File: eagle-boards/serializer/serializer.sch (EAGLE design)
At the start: 8 parts, among them IC1 74LS93N, IC2 74LS151N, IC3 74LS86N, IC4 74LS04N

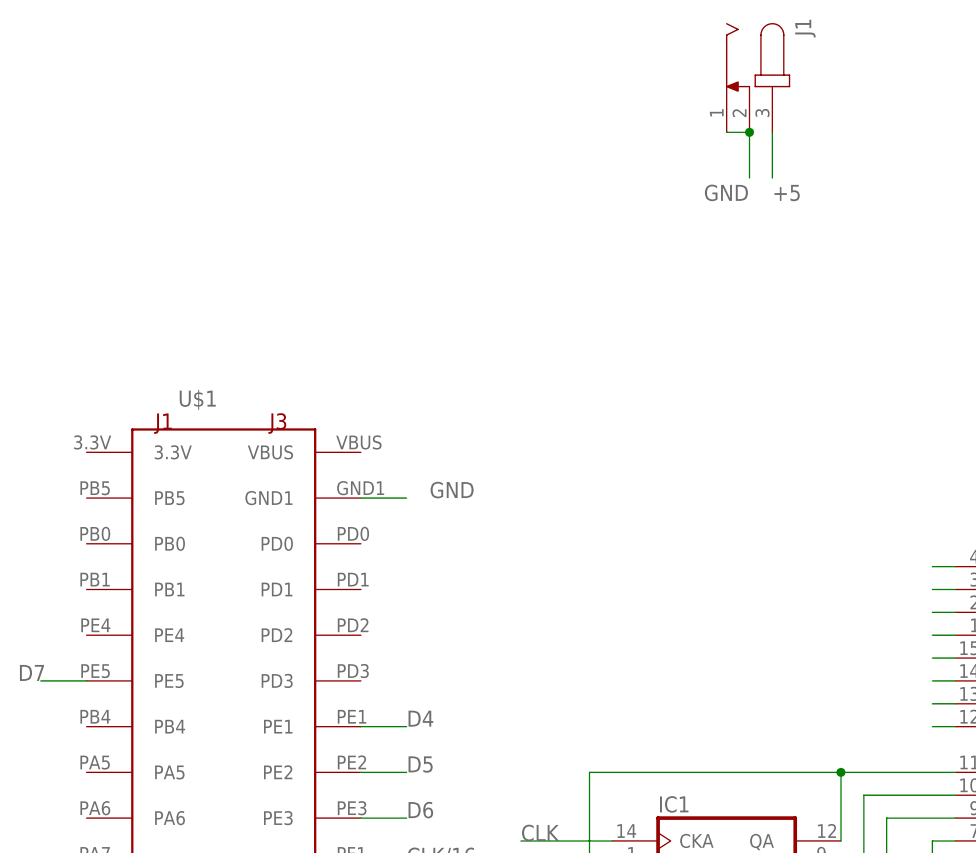
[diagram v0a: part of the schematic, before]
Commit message: Transmit code working with PLL
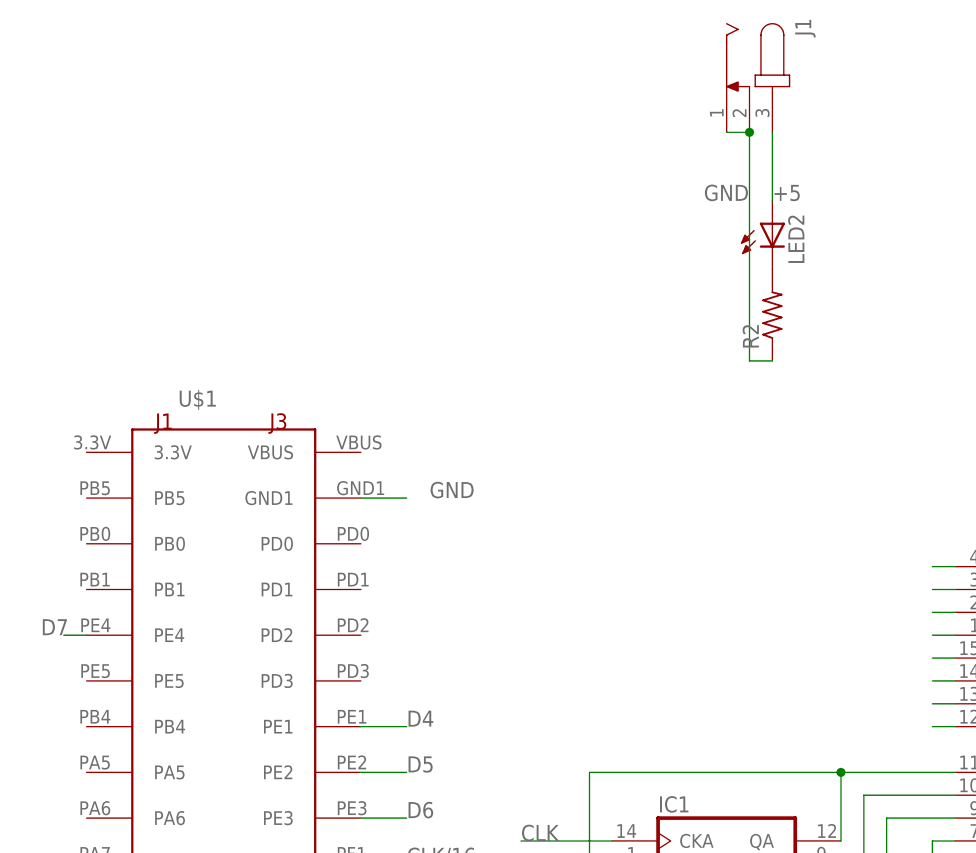
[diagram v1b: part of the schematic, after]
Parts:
- added LED2: (no value), led:LED5MM
- added R2: (no value), rcl:R-US_0207/10
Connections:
- new net N$2: LED2.C, R2.2
- net +5: now also LED2.A
- net D7: now also U$1.PE4; no longer U$1.PE5
- net GND: now also R2.1
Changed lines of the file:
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@@
 <part name="R1" library="rcl" deviceset="R-TRIMM" device="3296Y"/>
 <part name="J1" library="con-jack" deviceset="JACK-PLUG" device="0"/>
+<part name="R2" library="rcl" deviceset="R-US_" device="0207/10"/>
+<part name="LED2" library="led" deviceset="LED" device="5MM"/>
 </parts>
 <sheets>
@@
 <instance part="R1" gate="G$1" x="152.4" y="99.06" rot="R270"/>
 <instance part="J1" gate="G$1" x="45.72" y="142.24" rot="R270"/>
+<instance part="R2" gate="G$1" x="48.26" y="116.84" rot="R90"/>
+<instance part="LED2" gate="G$1" x="48.26" y="127"/>
 </instances>
 <busses>
@@
 <segment>
 <pinref part="J1" gate="G$1" pin="2"/>
-<wire x1="45.72" y1="137.16" x2="45.72" y2="132.08" width="0.1524" layer="91"/>
 <label x="40.64" y="129.54" size="1.778" layer="95"/>
 <pinref part="J1" gate="G$1" pin="1"/>
 <wire x1="43.18" y1="137.16" x2="45.72" y2="137.16" width="0.1524" layer="91"/>
 <junction x="45.72" y="137.16"/>
+<pinref part="R2" gate="G$1" pin="1"/>
+<wire x1="48.26" y1="111.76" x2="45.72" y2="111.76" width="0.1524" layer="91"/>
+<wire x1="45.72" y1="111.76" x2="45.72" y2="137.16" width="0.1524" layer="91"/>
 </segment>
 </net>
@@
 <segment>
 <pinref part="J1" gate="G$1" pin="3"/>
-<wire x1="48.26" y1="137.16" x2="48.26" y2="132.08" width="0.1524" layer="91"/>
+<wire x1="48.26" y1="137.16" x2="48.26" y2="129.54" width="0.1524" layer="91"/>
 <label x="48.26" y="129.54" size="1.778" layer="95"/>
+<pinref part="LED2" gate="G$1" pin="A"/>
 </segment>
 </net>
@@
 </segment>
 <segment>
-<pinref part="U$1" gate="G$1" pin="PE5"/>
-<wire x1="-27.94" y1="76.2" x2="-33.02" y2="76.2" width="0.1524" layer="91"/>
-<label x="-35.56" y="76.2" size="1.778" layer="95"/>
+<pinref part="U$1" gate="G$1" pin="PE4"/>
+<wire x1="-27.94" y1="81.28" x2="-30.48" y2="81.28" width="0.1524" layer="91"/>
+<label x="-33.02" y="81.28" size="1.778" layer="95"/>
 </segment>
 </net>
@@
 </segment>
 </net>
+<net name="N$2" class="0">
+<segment>
+<pinref part="R2" gate="G$1" pin="2"/>
+<pinref part="LED2" gate="G$1" pin="C"/>
+</segment>
+</net>
